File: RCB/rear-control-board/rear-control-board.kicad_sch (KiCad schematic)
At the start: 15 parts, among them J1 Conn_01x23, J2 Conn_01x14, J3 Conn_01x08, K1 T9VV1K15-12S, U3 R-78B5.0-2.0

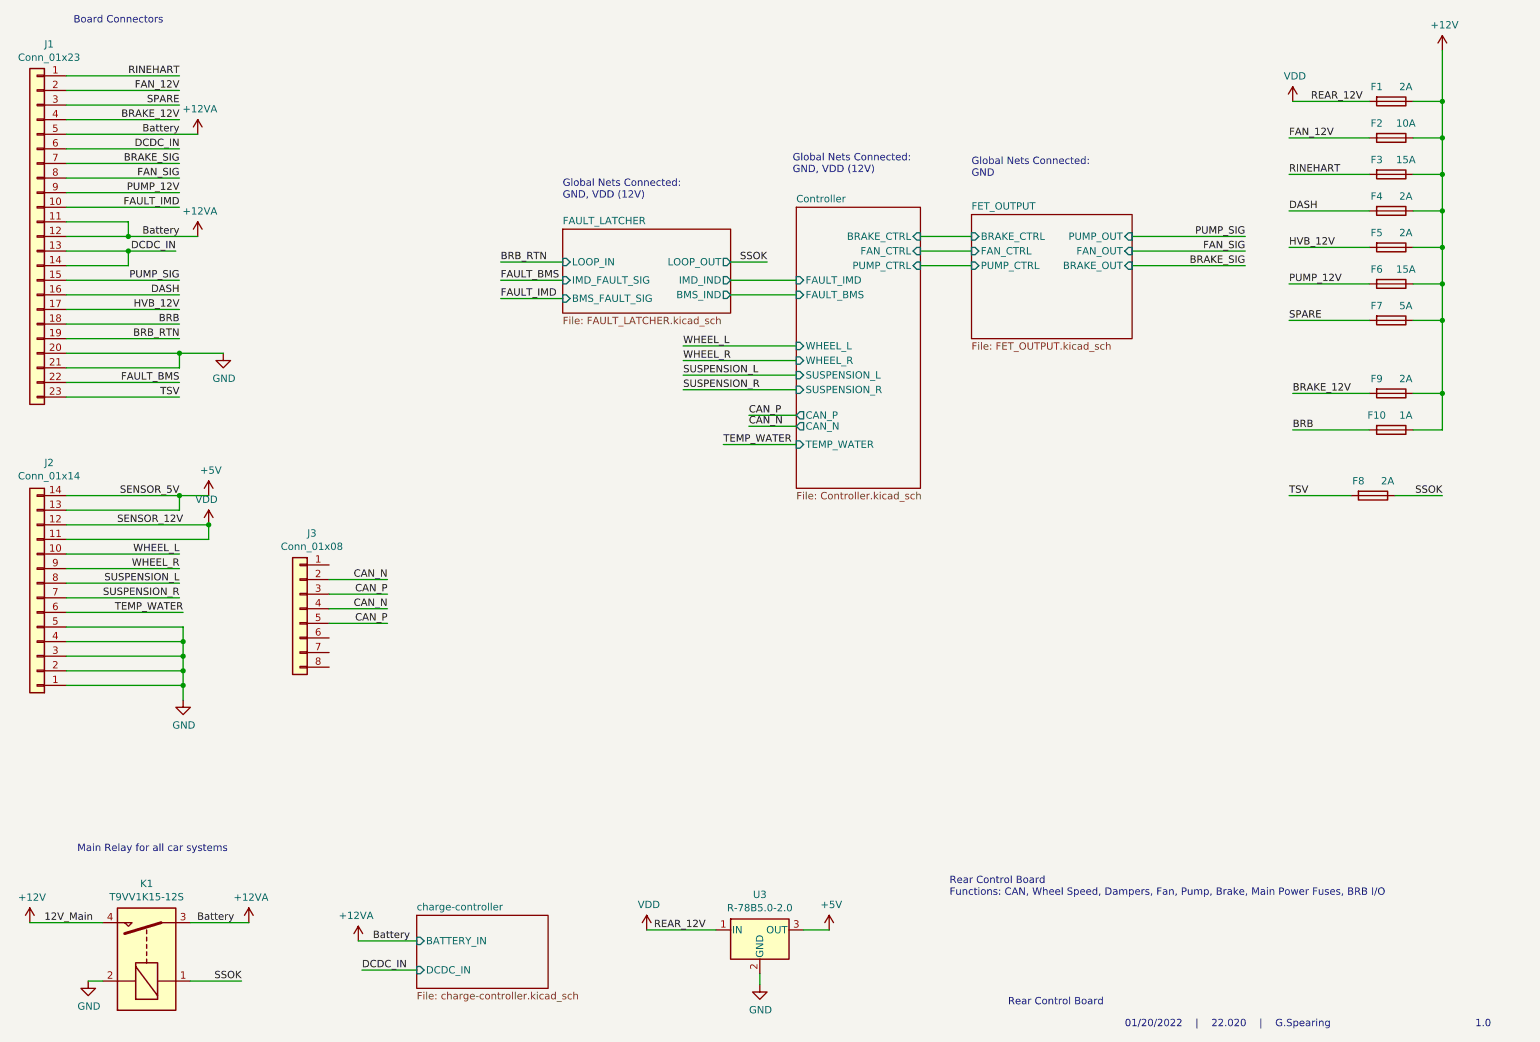
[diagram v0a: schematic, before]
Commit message: working on layout
Updating traces for RCB and organizing HVB
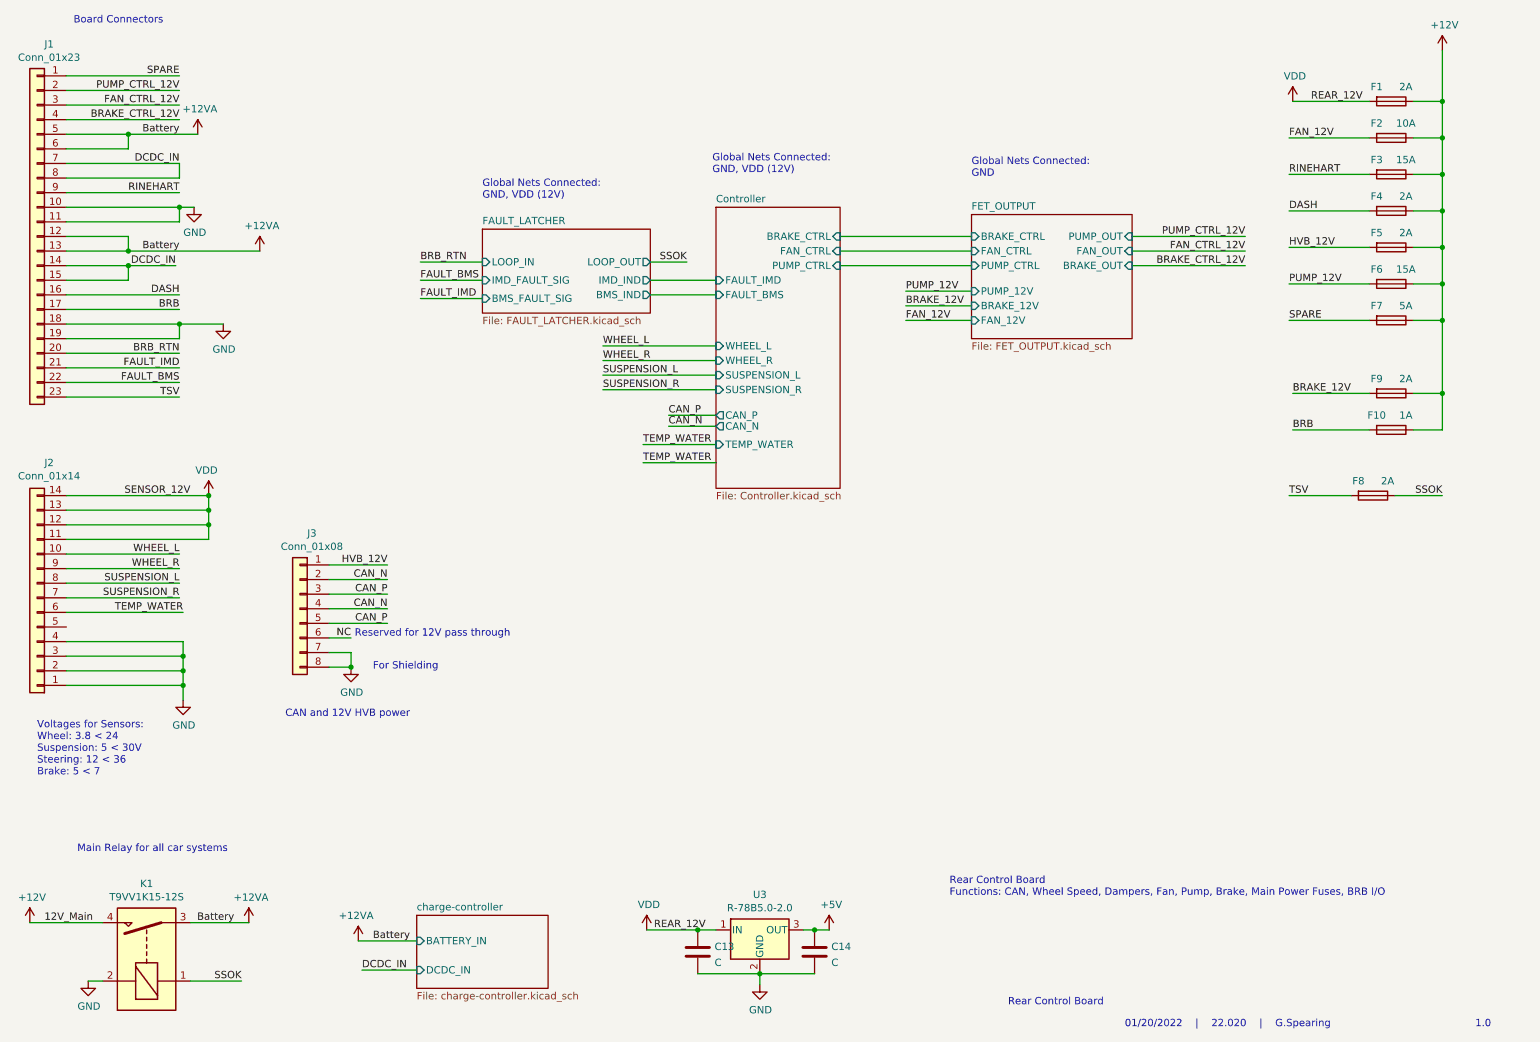
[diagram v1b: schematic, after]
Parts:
- added C13, C14: C, Capacitor_SMD:C_0603_1608Metric_Pad1.08x0.95mm_HandSolder, symbol Device:C
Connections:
- net BRAKE_SIG is gone; now on net DCDC_IN: J1.7 (Pin_7)
- net FAN_SIG is gone; now on net DCDC_IN: J1.8 (Pin_8)
- net PUMP_SIG is gone; now on net DCDC_IN: J1.15 (Pin_15)
- net +12VA: now also J1.13 (Pin_13), J1.6 (Pin_6); no longer J1.11 (Pin_11)
- net +5V: now also C14.1; no longer J2.13 (Pin_13), J2.14 (Pin_14)
- net BRAKE_12V: no longer J1.4 (Pin_4)
- net BRB: now also J1.17 (Pin_17); no longer J1.18 (Pin_18)
- net BRB_RTN: now also J1.20 (Pin_20); no longer J1.19 (Pin_19)
- net DCDC_IN: no longer J1.13 (Pin_13), J1.6 (Pin_6)
- net FAN_12V: no longer J1.2 (Pin_2)
- net FAULT_IMD: now also J1.21 (Pin_21); no longer J1.10 (Pin_10)
- net GND: now also J1.10 (Pin_10), J1.11 (Pin_11), J1.18 (Pin_18), J1.19 (Pin_19), J3.7 (Pin_7), J3.8 (Pin_8), C13.2, C14.2; no longer J1.20 (Pin_20), J1.21 (Pin_21), J2.5 (Pin_5)
- net HVB_12V: now also J3.1 (Pin_1); no longer J1.17 (Pin_17)
- net PUMP_12V: no longer J1.9 (Pin_9)
- net RINEHART: now also J1.9 (Pin_9); no longer J1.1 (Pin_1)
- net SPARE: now also J1.1 (Pin_1); no longer J1.3 (Pin_3)
- net VDD: now also J2.13 (Pin_13), J2.14 (Pin_14), C13.1
- net NC: now reaches J3.6 (Pin_6)
- new net BRAKE_CTRL_12V: J1.4 (Pin_4)
- new net FAN_CTRL_12V: J1.3 (Pin_3)
- new net PUMP_CTRL_12V: J1.2 (Pin_2)
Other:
- sheet FET_OUTPUT ports: added BRAKE_12V, FAN_12V, PUMP_12V; removed none
- note added: "CAN and 12V HVB power"
- note added: "For Shielding"
- note added: "Reserved for 12V pass through"
- note added: "Voltages for Sensors: Wheel: 3.8 < 24 Suspension: 5 < 30V Steering: 12 < 36 Brake: 5 < 7"

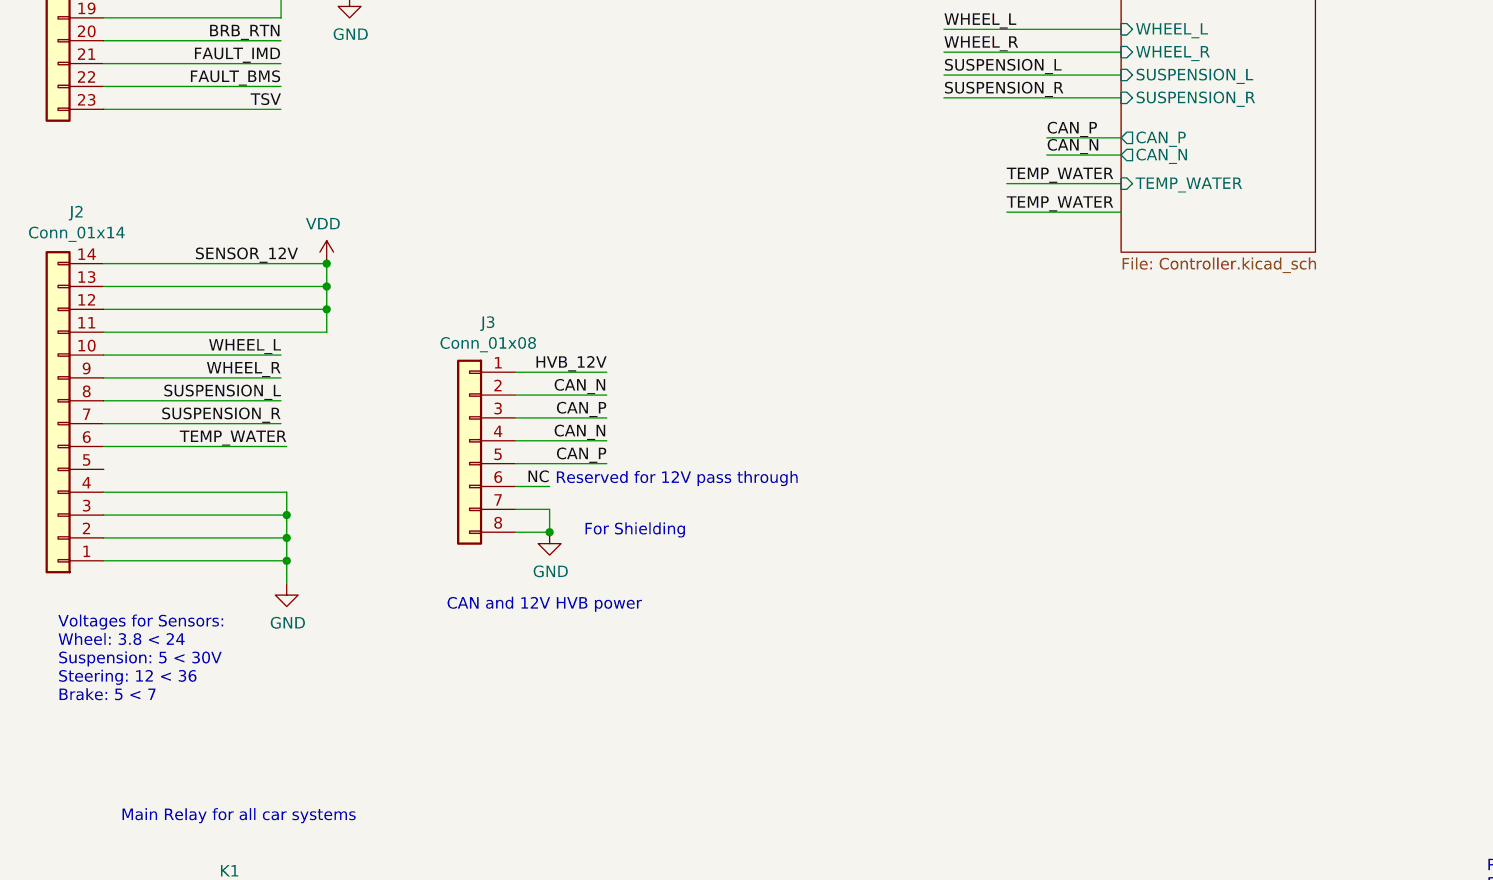
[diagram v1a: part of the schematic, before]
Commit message: finishing layout placement
Still need to route wires
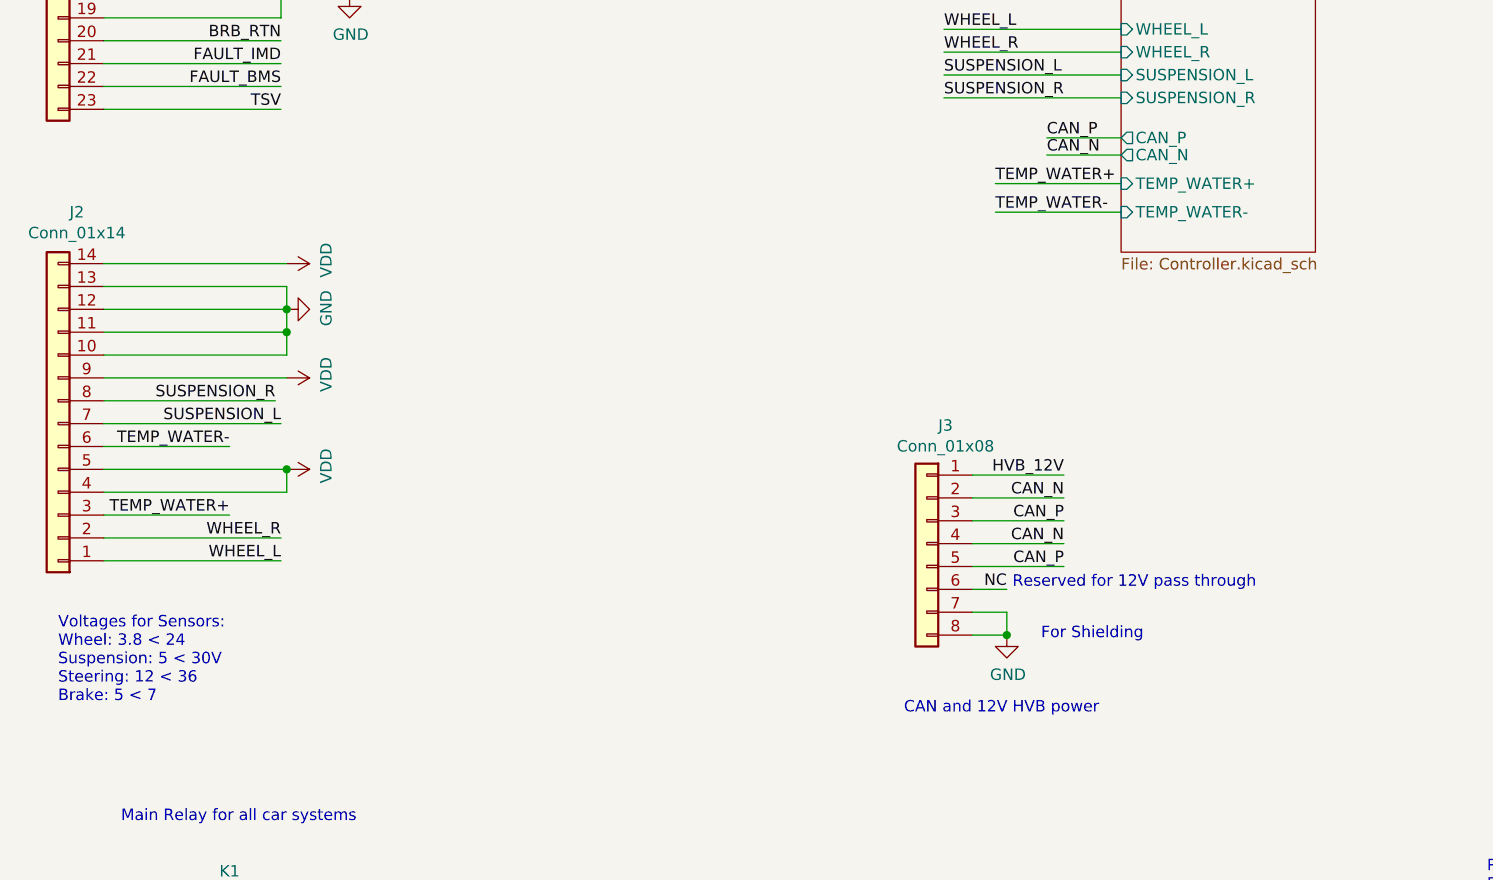
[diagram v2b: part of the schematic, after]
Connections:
- net GND: now also J2.10 (Pin_10), J2.11 (Pin_11), J2.12 (Pin_12), J2.13 (Pin_13); no longer J2.1 (Pin_1), J2.2 (Pin_2), J2.3 (Pin_3), J2.4 (Pin_4)
- net SUSPENSION_L: now also J2.7 (Pin_7); no longer J2.8 (Pin_8)
- net SUSPENSION_R: now also J2.8 (Pin_8); no longer J2.7 (Pin_7)
- net VDD: now also J2.4 (Pin_4), J2.5 (Pin_5), J2.9 (Pin_9); no longer J2.11 (Pin_11), J2.12 (Pin_12), J2.13 (Pin_13)
- net WHEEL_L: now also J2.1 (Pin_1); no longer J2.10 (Pin_10)
- net WHEEL_R: now also J2.2 (Pin_2); no longer J2.9 (Pin_9)
- net TEMP_WATER renamed TEMP_WATER-
- new net TEMP_WATER+: J2.3 (Pin_3)
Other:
- sheet Controller ports: added TEMP_WATER+, TEMP_WATER-; removed TEMP_WATER
- moved on the sheet: J3

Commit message: adding mounting holes
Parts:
- added H1, H2: MountingHole, MountingHole:MountingHole_3.2mm_M3, symbol Mechanical:MountingHole
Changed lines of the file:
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@@
     (pin "2")
+  )
+  (symbol (lib_id "Mechanical:MountingHole") (at 225.425 156.845 0) (unit 1)
+    (in_bom yes) (on_board yes) (fields_autoplaced)
+    (property "Reference" "H1" (id 0) (at 227.965 155.9365 0)
+      (effects (font (size 1.27 1.27)) (justify left))
+    )
+    (property "Value" "MountingHole" (id 1) (at 227.965 158.7116 0)
+      (effects (font (size 1.27 1.27)) (justify left))
+    )
+    (property "Footprint" "MountingHole:MountingHole_3.2mm_M3" (id 2) (at 225.425 156.845 0)
+      (effects (font (size 1.27 1.27)) hide)
+    )
+    (property "Datasheet" "~" (id 3) (at 225.425 156.845 0)
+      (effects (font (size 1.27 1.27)) hide)
+    )
   )
   (symbol (lib_id "power:VDD") (at 44.45 124.46 270) (mirror x) (unit 1)
@@
     )
     (pin "1")
+  )
+  (symbol (lib_id "Mechanical:MountingHole") (at 245.745 156.845 0) (unit 1)
+    (in_bom yes) (on_board yes) (fields_autoplaced)
+    (property "Reference" "H2" (id 0) (at 248.285 155.9365 0)
+      (effects (font (size 1.27 1.27)) (justify left))
+    )
+    (property "Value" "MountingHole" (id 1) (at 248.285 158.7116 0)
+      (effects (font (size 1.27 1.27)) (justify left))
+    )
+    (property "Footprint" "MountingHole:MountingHole_3.2mm_M3" (id 2) (at 245.745 156.845 0)
+      (effects (font (size 1.27 1.27)) hide)
+    )
+    (property "Datasheet" "~" (id 3) (at 245.745 156.845 0)
+      (effects (font (size 1.27 1.27)) hide)
+    )
   )
   (sheet (at 137.16 51.435) (size 21.59 48.895) (fields_autoplaced)
@@
       (reference "F11") (unit 1) (value "20A") (footprint "AERO_Footprints:Fuseholder_Blade_Mini_Keystone_3568")
     )
+    (path "/be777c60-066a-42c5-a3fc-a93a51cb5f92"
+      (reference "H1") (unit 1) (value "MountingHole") (footprint "MountingHole:MountingHole_3.2mm_M3")
+    )
+    (path "/fc429a50-a0c7-46e0-83ea-3e5edfb07375"
+      (reference "H2") (unit 1) (value "MountingHole") (footprint "MountingHole:MountingHole_3.2mm_M3")
+    )
     (path "/00000000-0000-0000-0000-00006250f2e8"

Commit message: updating can pinouts
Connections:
- net NC is gone; now on net CAN_N: J3.6 (Pin_6)
- net CAN_P: now also J3.7 (Pin_7)
- net GND: no longer J3.7 (Pin_7)
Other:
- note added: "CAN goes to HVB and Rinehart"
- note removed: "Reserved for 12V pass through"
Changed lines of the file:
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@@
   (junction (at 133.985 177.165) (diameter 0) (color 0 0 0 0)
   )
-  (junction (at 124.46 142.875) (diameter 0) (color 0 0 0 0)
-  )
   (junction (at 34.925 61.595) (diameter 0) (color 0 0 0 0)
   )
@@
     (stroke (width 0) (type default) (color 0 0 0 0))
   )
-  (wire (pts (xy 124.46 140.335) (xy 120.65 140.335))
-    (stroke (width 0) (type default) (color 0 0 0 0))
-  )
   (wire (pts (xy 24.13 69.215) (xy 43.815 69.215))
     (stroke (width 0) (type default) (color 0 0 0 0))
@@
     (stroke (width 0) (type default) (color 0 0 0 0))
   )
-  (wire (pts (xy 120.65 137.795) (xy 124.46 137.795))
-    (stroke (width 0) (type default) (color 0 0 0 0))
-  )
   (wire (pts (xy 130.81 132.715) (xy 120.65 132.715))
     (stroke (width 0) (type default) (color 0 0 0 0))
@@
     (stroke (width 0) (type default) (color 0 0 0 0))
   )
+  (wire (pts (xy 130.81 137.795) (xy 120.65 137.795))
+    (stroke (width 0) (type default) (color 0 0 0 0))
+  )
   (wire (pts (xy 34.925 61.595) (xy 24.13 61.595))
     (stroke (width 0) (type default) (color 0 0 0 0))
@@
     (stroke (width 0) (type default) (color 0 0 0 0))
   )
-  (wire (pts (xy 124.46 142.875) (xy 124.46 140.335))
-    (stroke (width 0) (type default) (color 0 0 0 0))
-  )
   (wire (pts (xy 132.08 60.96) (xy 125.73 60.96))
     (stroke (width 0) (type default) (color 0 0 0 0))
@@
   )
   (wire (pts (xy 154.305 177.165) (xy 152.4 177.165))
+    (stroke (width 0) (type default) (color 0 0 0 0))
+  )
+  (wire (pts (xy 130.81 140.335) (xy 120.65 140.335))
     (stroke (width 0) (type default) (color 0 0 0 0))
   )
@@
     (effects (font (size 1.27 1.27)) (justify left bottom))
   )
-  (text "Reserved for 12V pass through" (at 125.095 137.795 0)
-    (effects (font (size 1.27 1.27)) (justify left bottom))
-  )
   (text "01/20/2022    |    22.020    |    G.Spearing" (at 208.28 194.31 0)
     (effects (font (size 1.27 1.27)) (justify left bottom))
@@
     (effects (font (size 1.27 1.27)) (justify left bottom))
   )
+  (text "CAN goes to HVB\nand Rinehart" (at 133.985 131.445 0)
+    (effects (font (size 1.27 1.27)) (justify left bottom))
+  )
   (text "For Shielding" (at 128.27 143.51 0)
     (effects (font (size 1.27 1.27)) (justify left bottom))
@@
     (effects (font (size 1.27 1.27)) (justify right bottom))
   )
-  (label "NC" (at 124.46 137.795 180)
-    (effects (font (size 1.27 1.27)) (justify right bottom))
-  )
   (label "FAULT_IMD" (at 43.815 79.375 180)
     (effects (font (size 1.27 1.27)) (justify right bottom))
@@
     (effects (font (size 1.27 1.27)) (justify left bottom))
   )
+  (label "CAN_P" (at 130.81 140.335 180)
+    (effects (font (size 1.27 1.27)) (justify right bottom))
+  )
   (label "SUSPENSION_L" (at 43.815 119.38 180)
     (effects (font (size 1.27 1.27)) (justify right bottom))
@@
     (effects (font (size 1.27 1.27)) (justify right bottom))
   )
+  (label "CAN_N" (at 130.81 137.795 180)
+    (effects (font (size 1.27 1.27)) (justify right bottom))
+  )
